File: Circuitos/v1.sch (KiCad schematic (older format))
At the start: 10 parts, among them J1 12v, J2 Inyectores, J3 SIL10, Q1 IRFZ44N, U2 PC817

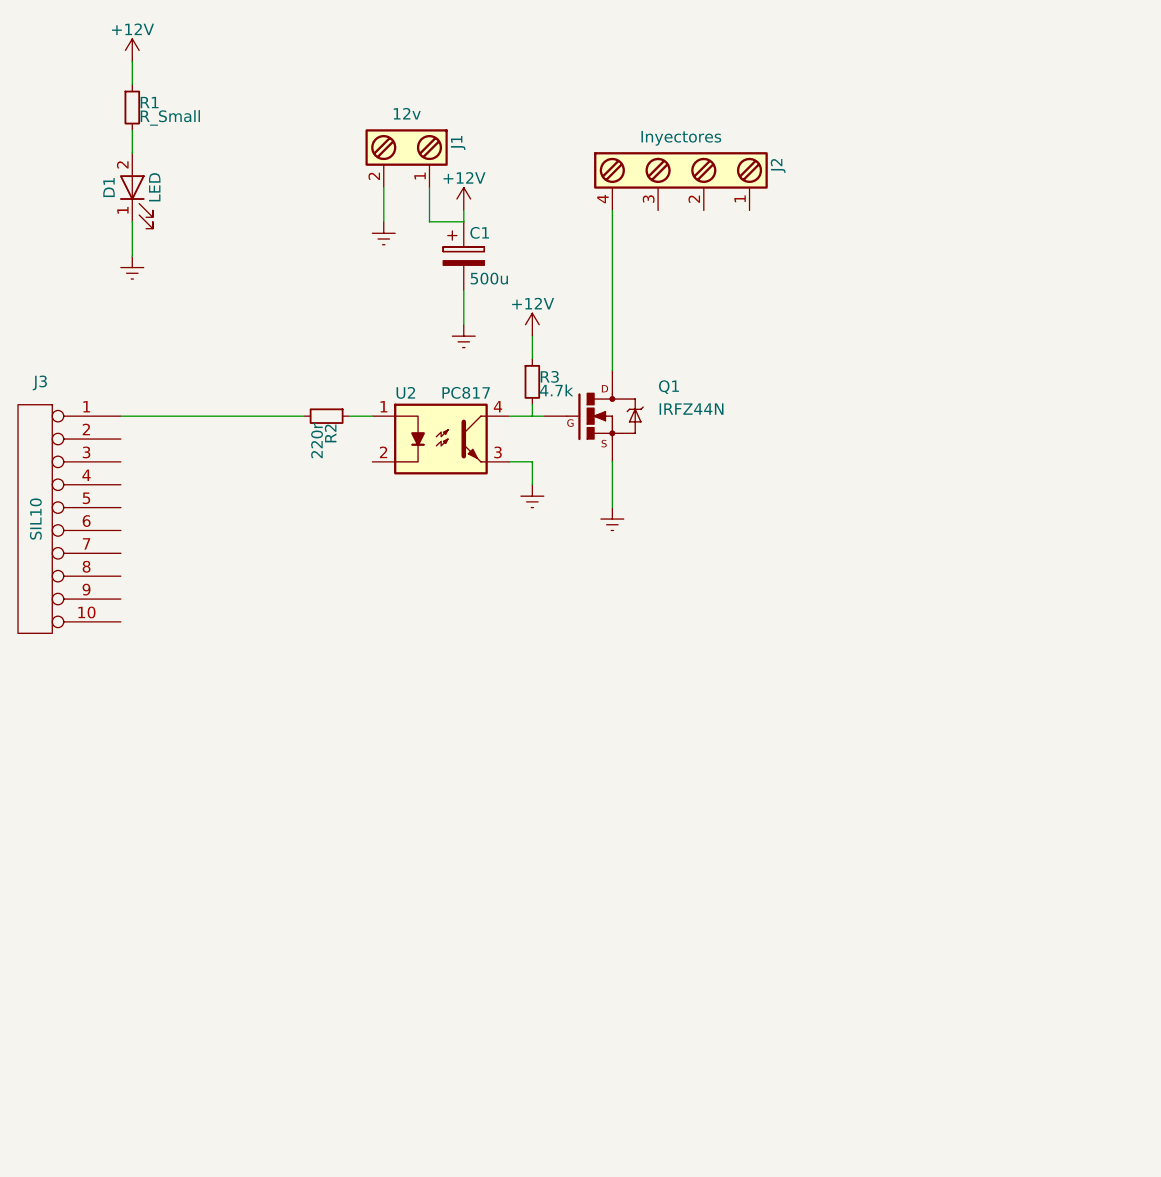
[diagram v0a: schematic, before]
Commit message: Agregada funcion de sincronizacion y cambios en planos
ademas de la funcion de sincronizacion ya termine el plano del sistema
de control de los inyectores, falta PCB :P
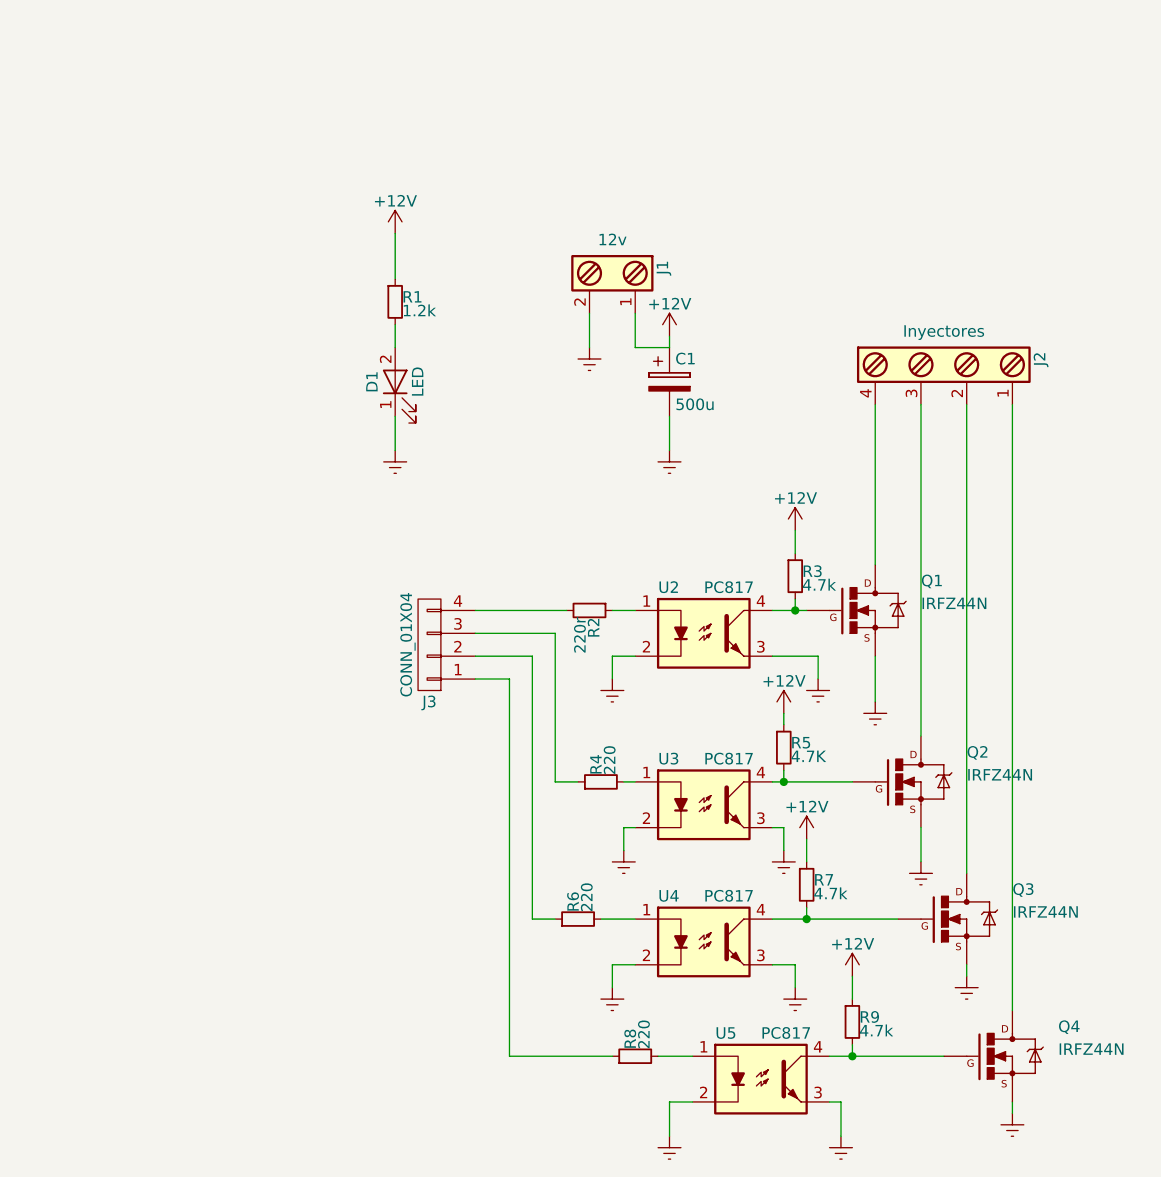
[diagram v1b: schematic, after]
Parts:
- removed J3: SIL10, symbol SIL10
- added J3: CONN_01X04, Connectors_JST:JST_EH_B04B-EH-A_04x2.50mm_Straight, symbol CONN_01X04
- added Q2, Q3, Q4: IRFZ44N, IRFZ44N:TO-220, symbol IRFZ44N
- added R4, R6, R8: 220, Resistors_THT:R_Axial_DIN0204_L3.6mm_D1.6mm_P2.54mm_Vertical, symbol R_Small
- added R5: 4.7K, Resistors_THT:R_Axial_DIN0204_L3.6mm_D1.6mm_P2.54mm_Vertical, symbol R_Small
- added R7, R9: 4.7k, Resistors_THT:R_Axial_DIN0204_L3.6mm_D1.6mm_P2.54mm_Vertical, symbol R_Small
- added U3, U4, U5: PC817, Housings_DIP:DIP-4_W7.62mm, symbol PC817
- C1: footprint (none) -> Capacitors_THT:CP_Radial_D8.0mm_P3.80mm
- D1: footprint (none) -> LEDs:LED_D3.0mm_FlatTop
- J1: footprint (none) -> Connectors_Terminal_Blocks:TerminalBlock_Pheonix_PT-3.5mm_2pol
- J2: footprint (none) -> Connectors_Terminal_Blocks:TerminalBlock_Pheonix_PT-3.5mm_4pol
- Q1: footprint TO-220 -> IRFZ44N:TO-220
- R1: value R_Small -> 1.2k; footprint (none) -> Resistors_THT:R_Axial_DIN0204_L3.6mm_D1.6mm_P2.54mm_Vertical
- R2: footprint (none) -> Resistors_THT:R_Axial_DIN0204_L3.6mm_D1.6mm_P2.54mm_Vertical
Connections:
- wire segments 17 -> 58
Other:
- moved on the sheet: C1, D1, J1, J2, Q1, R1, R2, R3, U2
